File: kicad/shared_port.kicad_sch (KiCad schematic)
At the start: 44 parts, among them J1 Keyboard (2x10 box), J2 SNES pad, J3 SNES pad, J4 SD (SPI), J5 PS/2 kbd + mouse, U37 SN74HC574N, U38 ATF22V10C-7PX, U39 SN74F541N

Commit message: Kit footprints: DIP sockets with puller room and part number, resistors with value
Justin: put the chip-puller room in the socket footprints (User.Eco1,
2.5 mm past each end) and the part number in silkscreen between the pin
rows; resistors get their value in silkscreen on the body. New
gen_kicad_kit_footprints.py derives them from KiCad's stock footprints;
schematic, symbols, BOM and PDFs now name them. The board file is left
as is (Justin is editing it): Update PCB from Schematic swaps them in.

Co-Authored-By: Claude Opus 5.5 (1M context) <noreply@anthropic.com>
Claude-Session: https://claude.ai/code/session_01JnVuvUvdWezUUU6Sgmg16H
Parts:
- R40, R41, R42, R43, R44, R45, R46, R47, R48, R49, R50, R55: footprint Resistor_THT:R_Axial_DIN0207_L6.3mm_D2.5mm_P10.16mm_Horizontal -> placard:R_Axial_DIN0207_L6.3mm_D2.5mm_P10.16mm_Horizontal_Value
- U37, U39: footprint Package_DIP:DIP-20_W7.62mm -> placard:DIP-20_W7.62mm_Socket_Puller
- U38: footprint Package_DIP:DIP-24_W7.62mm -> placard:DIP-24_W7.62mm_Socket_Puller

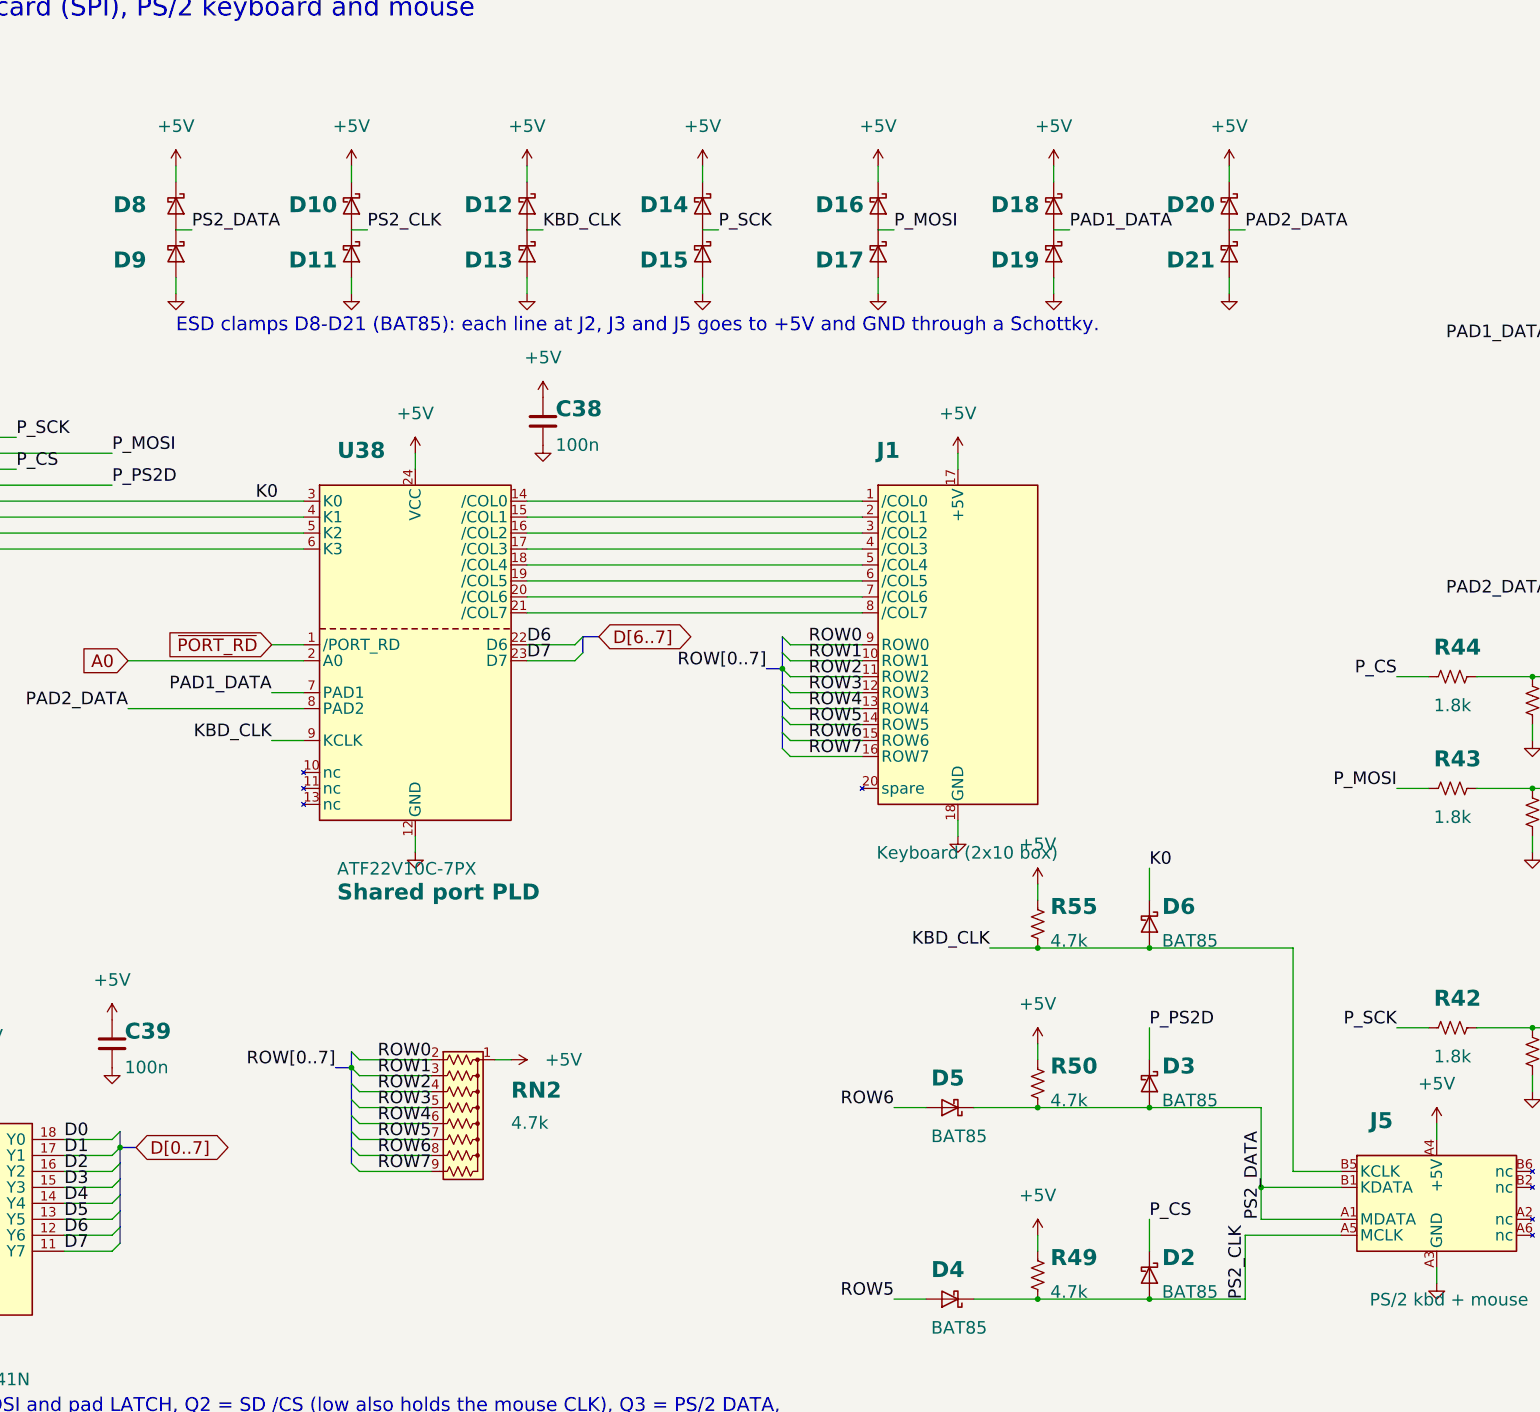
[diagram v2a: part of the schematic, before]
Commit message: Remove the ESD clamps from PS/2, SNES and VGA
Justin decided to take the BAT85 steering pairs out entirely: D8-D21
(shared port sheet) and D22-D25 (video sheet sync lines), 18 diodes.
D7 (TVS on VBUS) stays.

The remaining diodes are renumbered so every kind is numbered from 1 with
no gaps: D26 -> D8 (relay coil), D27-D29 -> D9-D11 (tint BAT85),
D30-D35 -> D12-D17 (tint 1N4148).

The schematic generator now keeps each symbol's uuid from the files
already on disk (and RENUMBERED carries a renamed part's old uuid for one
run), so Update PCB from Schematic renames the renumbered footprints and
leaves every other footprint linked.  kicad/placard.kicad_pcb is not
touched.  BOM, PDFs (no bookmarks panel), placement lists and docs updated.

Co-Authored-By: Claude Opus 5.5 (1M context) <noreply@anthropic.com>
Claude-Session: https://claude.ai/code/session_01DRvpu48w1PN7avX3eFSFuQ
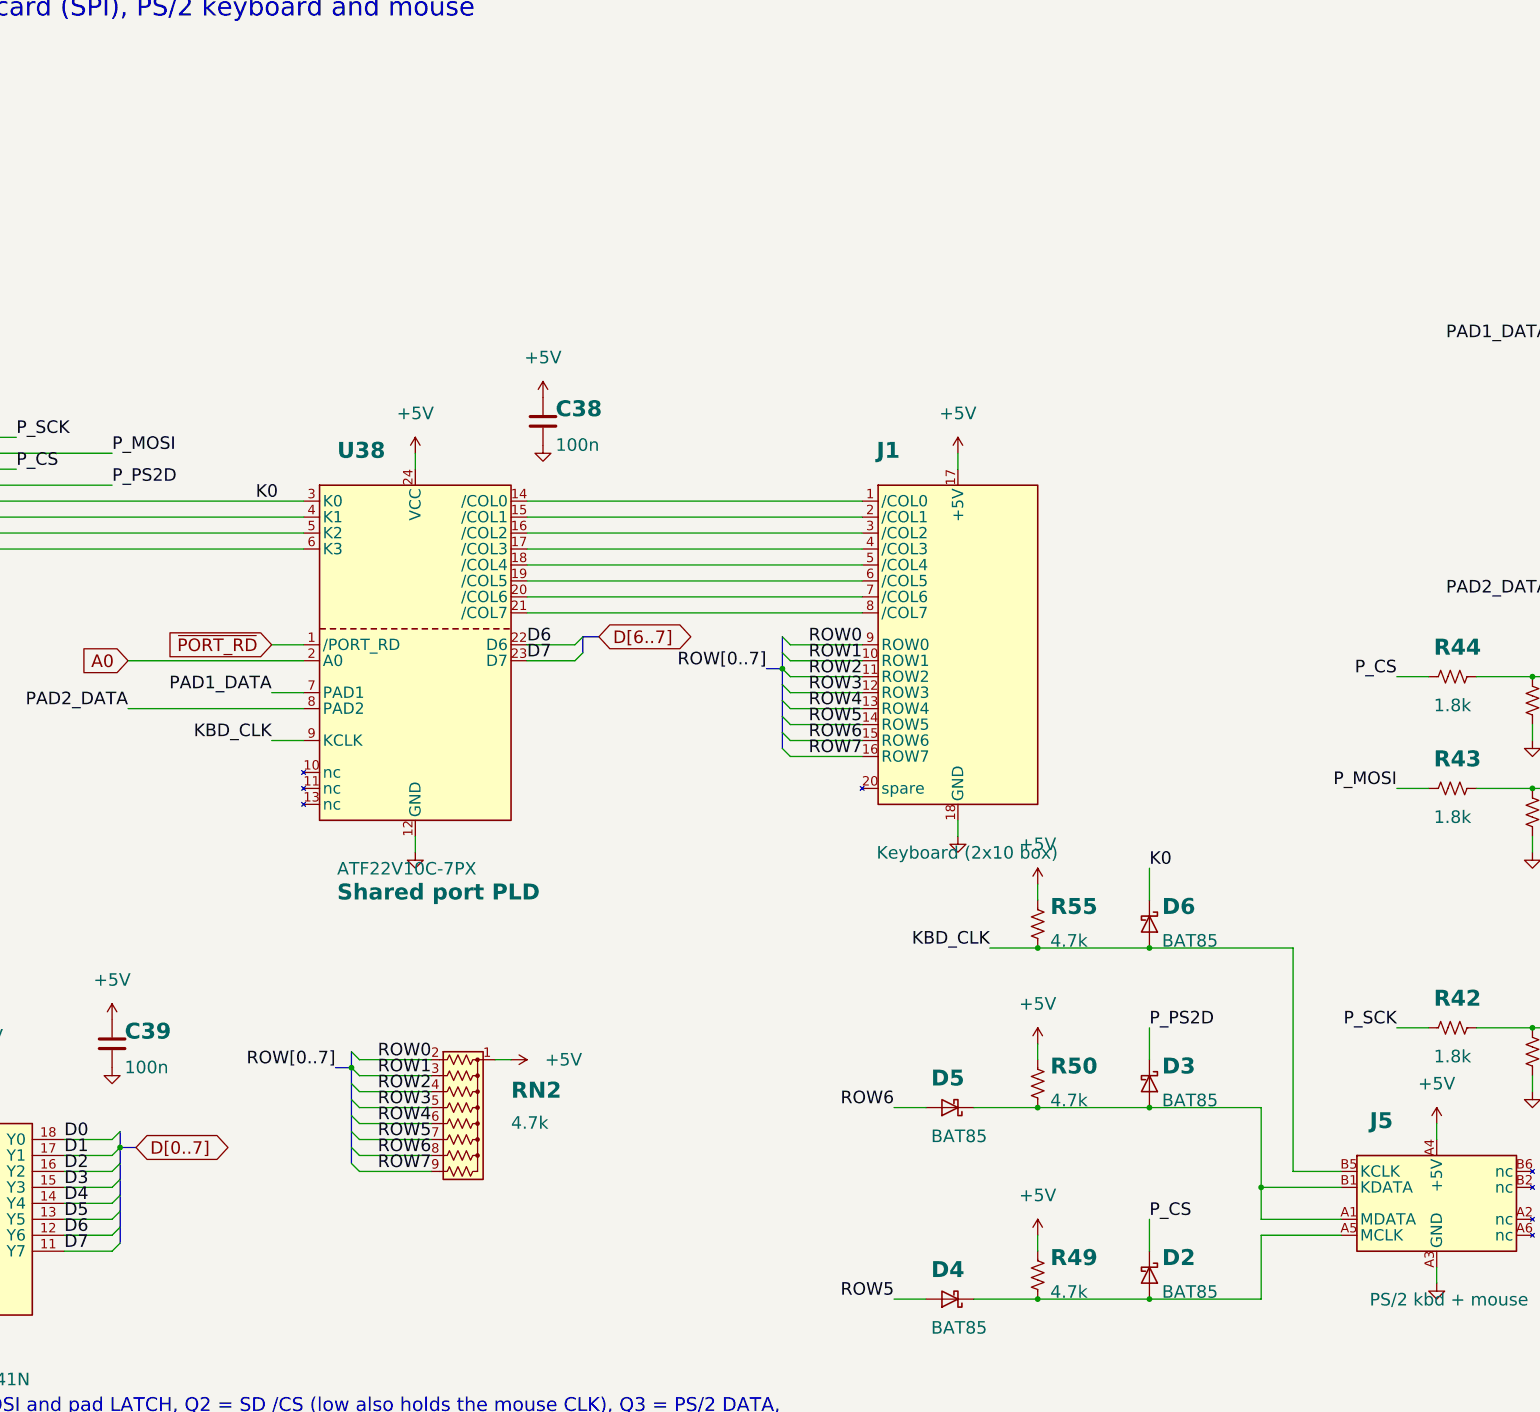
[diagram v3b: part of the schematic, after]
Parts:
- removed D10, D11, D12, D13, D14, D15, D16, D17, D18, D19, D20, D21, D8, D9: BAT85, Diode_THT:D_DO-35_SOD27_P7.62mm_Horizontal, symbol placard_std:D_Schottky
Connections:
- net PS2_CLK: no longer names the net of D2.2 (A), D4.1 (K), J5.A5 (MCLK), R49.2
- net PS2_DATA: no longer names the net of D3.2 (A), D5.1 (K), J5.A1 (MDATA), J5.B1 (KDATA), R50.2
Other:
- note removed: "ESD clamps D8-D21 (BAT85): each line at J2, J3 and J5 goes to +5V and GND through a Schottky."

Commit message: Add 3D models for the connectors, switches and polyfuse
Every connector/switch footprint in kicad/lib/placard.pretty now names a
STEP model in kicad/lib/placard.3dshapes via ${KIPRJMOD}, so the board shows
them in any KiCad version without a 3D library path.

- gen_kicad_3d_models.py (CadQuery) generates models at typical dimensions
  for J8 cart slot, J9-J12 expansion slots, J5 stacked PS/2, J6 audio jack,
  SW1 toggle, J4 SD socket, F1 polyfuse and J2/J3 SNES ports; leads are put
  on the footprint pads. KiCad's own models are copied for SW2, J7, J13.
- gen_kicad_connectors.py adds the model to its footprints and makes
  project copies of KiCad's SD, MF-RG300, PTS645 and DSUB-15-HD footprints
  (same pads) pointing at the project models; removes a duplicated block.
- Schematic, BOM and gen_kicad_pcb.py use the placard: copies for J4, J7,
  F1, SW2. kicad/placard.kicad_pcb is not touched.
- docs/connector_3d_models.png: KiCad STEP export of the footprints.

Co-Authored-By: Claude Opus 5.5 (1M context) <noreply@anthropic.com>
Claude-Session: https://claude.ai/code/session_011CYV6fCf1RGSdDoH9HuCKo
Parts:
- J4: footprint Connector_Card:SD_Kyocera_145638009511859+ -> placard:SD_Kyocera_145638009511859+
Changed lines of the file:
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@@
   (wire (pts (xy 350.52 170.18) (xy 347.98 170.18)) (stroke (width 0) (type default)))
   (symbol (lib_id "power:+3V3") (at 347.98 170.18 90) (unit 1) (in_bom yes) (on_board yes) (dnp no) (property "Reference" "#PWR1028" (at 347.98 170.18 0) (effects (font (size 1.27 1.27)) hide)) (property "Value" "+3V3" (at 338.68 170.18 90) (effects (font (size 2 2)))) (property "Footprint" "" (at 347.98 170.18 0) (effects (font (size 1.27 1.27)) hide)) (property "Datasheet" "" (at 347.98 170.18 0) (effects (font (size 1.27 1.27)) hide)) (pin "1") (instances (project "placard" (path "/e3450542-4ffc-59d4-a4a7-45636233928a/b3c80de0-82bc-5f69-87f9-71f84480d1b8" (reference "#PWR1028") (unit 1)))))
-  (symbol (lib_id "placard_std:SD_Card") (at 373.38 170.18 0) (unit 1) (in_bom yes) (on_board yes) (dnp no) (property "Reference" "J4" (at 353 153 0) (effects (font (size 2.54 2.54) bold) (justify left bottom))) (property "Value" "SD (SPI)" (at 353 187 0) (effects (font (size 2 2)) (justify left top))) (property "Footprint" "Connector_Card:SD_Kyocera_145638009511859+" (at 373.38 170.18 0) (effects (font (size 1.27 1.27)) hide)) (property "Datasheet" "http://portal.fciconnect.com/Comergent//fci/drawing/10067847.pdf" (at 373.38 170.18 0) (effects (font (size 1.27 1.27)) hide)) (property "Manufacturer" "Kyocera AVX" (at 373.38 170.18 0) (effects (font (size 1.27 1.27)) hide)) (property "MPN" "145638009511859+" (at 373.38 170.18 0) (effects (font (size 1.27 1.27)) hide)) (pin "1") (pin "10") (pin "11") (pin "12") (pin "13") (pin "2") (pin "3") (pin "4") (pin "5") (pin "6") (pin "7") (pin "8") (pin "9") (instances (project "placard" (path "/e3450542-4ffc-59d4-a4a7-45636233928a/b3c80de0-82bc-5f69-87f9-71f84480d1b8" (reference "J4") (unit 1)))))
+  (symbol (lib_id "placard_std:SD_Card") (at 373.38 170.18 0) (unit 1) (in_bom yes) (on_board yes) (dnp no) (property "Reference" "J4" (at 353 153 0) (effects (font (size 2.54 2.54) bold) (justify left bottom))) (property "Value" "SD (SPI)" (at 353 187 0) (effects (font (size 2 2)) (justify left top))) (property "Footprint" "placard:SD_Kyocera_145638009511859+" (at 373.38 170.18 0) (effects (font (size 1.27 1.27)) hide)) (property "Datasheet" "http://portal.fciconnect.com/Comergent//fci/drawing/10067847.pdf" (at 373.38 170.18 0) (effects (font (size 1.27 1.27)) hide)) (property "Manufacturer" "Kyocera AVX" (at 373.38 170.18 0) (effects (font (size 1.27 1.27)) hide)) (property "MPN" "145638009511859+" (at 373.38 170.18 0) (effects (font (size 1.27 1.27)) hide)) (pin "1") (pin "10") (pin "11") (pin "12") (pin "13") (pin "2") (pin "3") (pin "4") (pin "5") (pin "6") (pin "7") (pin "8") (pin "9") (instances (project "placard" (path "/e3450542-4ffc-59d4-a4a7-45636233928a/b3c80de0-82bc-5f69-87f9-71f84480d1b8" (reference "J4") (unit 1)))))
   (wire (pts (xy 350.52 177.8) (xy 345.44 177.8)) (stroke (width 0) (type default)))
   (wire (pts (xy 345.44 177.8) (xy 345.44 213.36)) (stroke (width 0) (type default)))
